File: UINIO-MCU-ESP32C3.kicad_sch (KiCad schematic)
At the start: 40 parts, among them J1 Conn_01x15_Male, J2 外接串行下载接口, J3 Conn_01x15_Male, SW1 复位按键, SW2 下载按键, U1 ME6211C33M5G-N, U2 W25Q128JVSSIQ, U3 ESP32-C3, U4 CH343P, Y1 40MHz

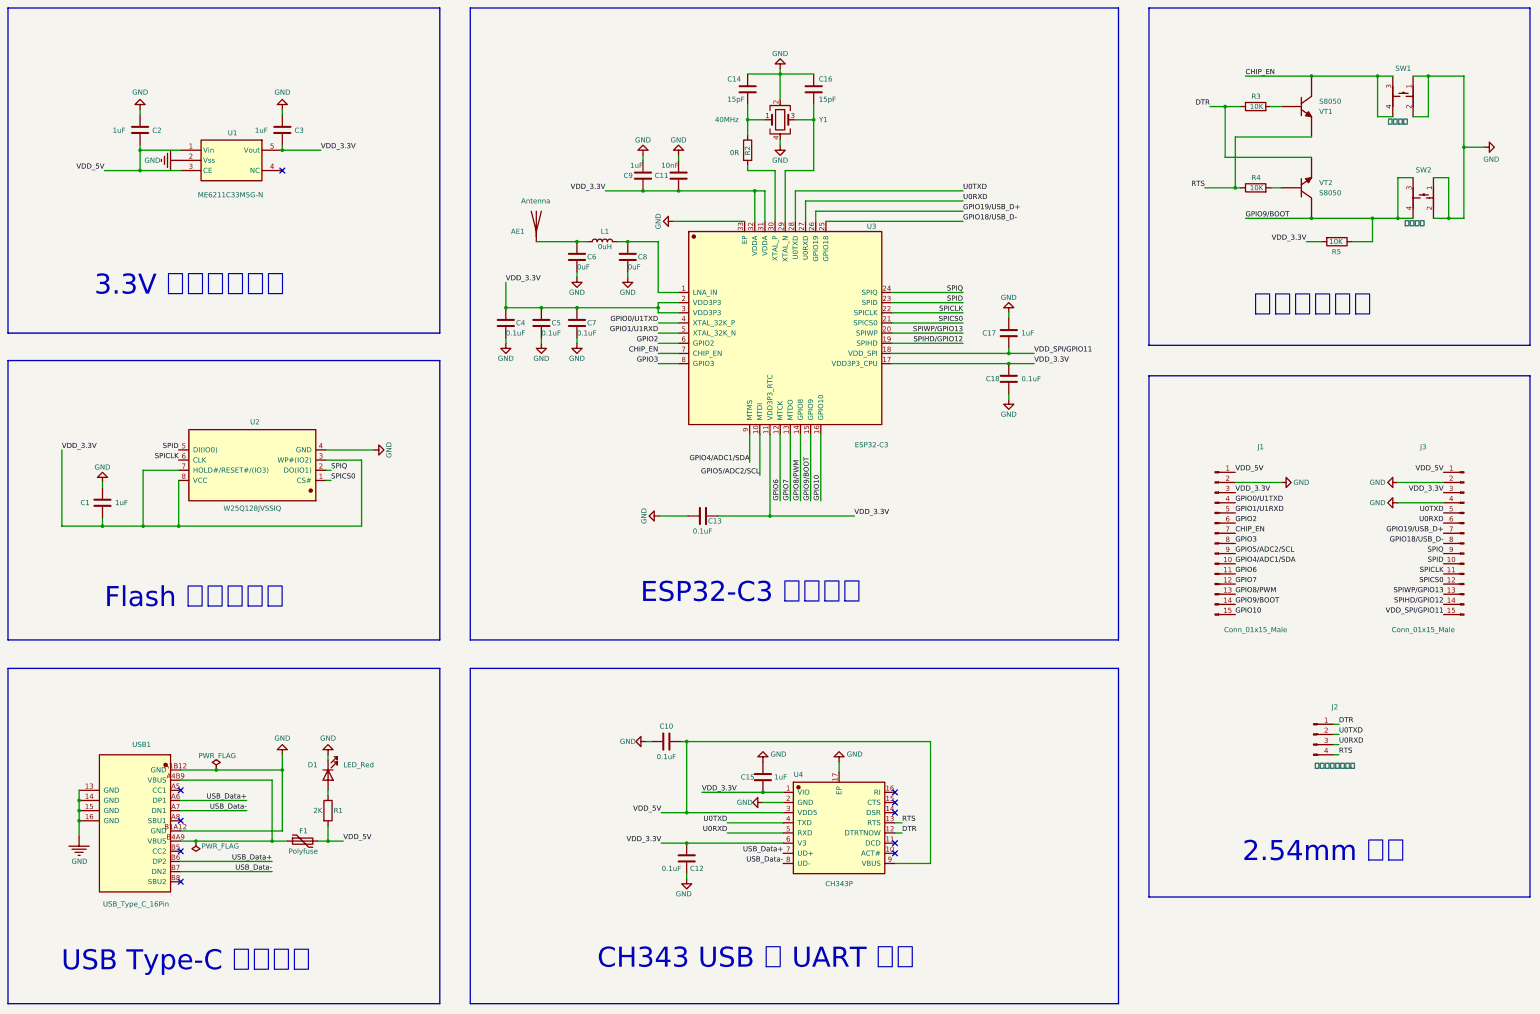
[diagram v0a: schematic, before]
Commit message: The schematic diagram is drawn.
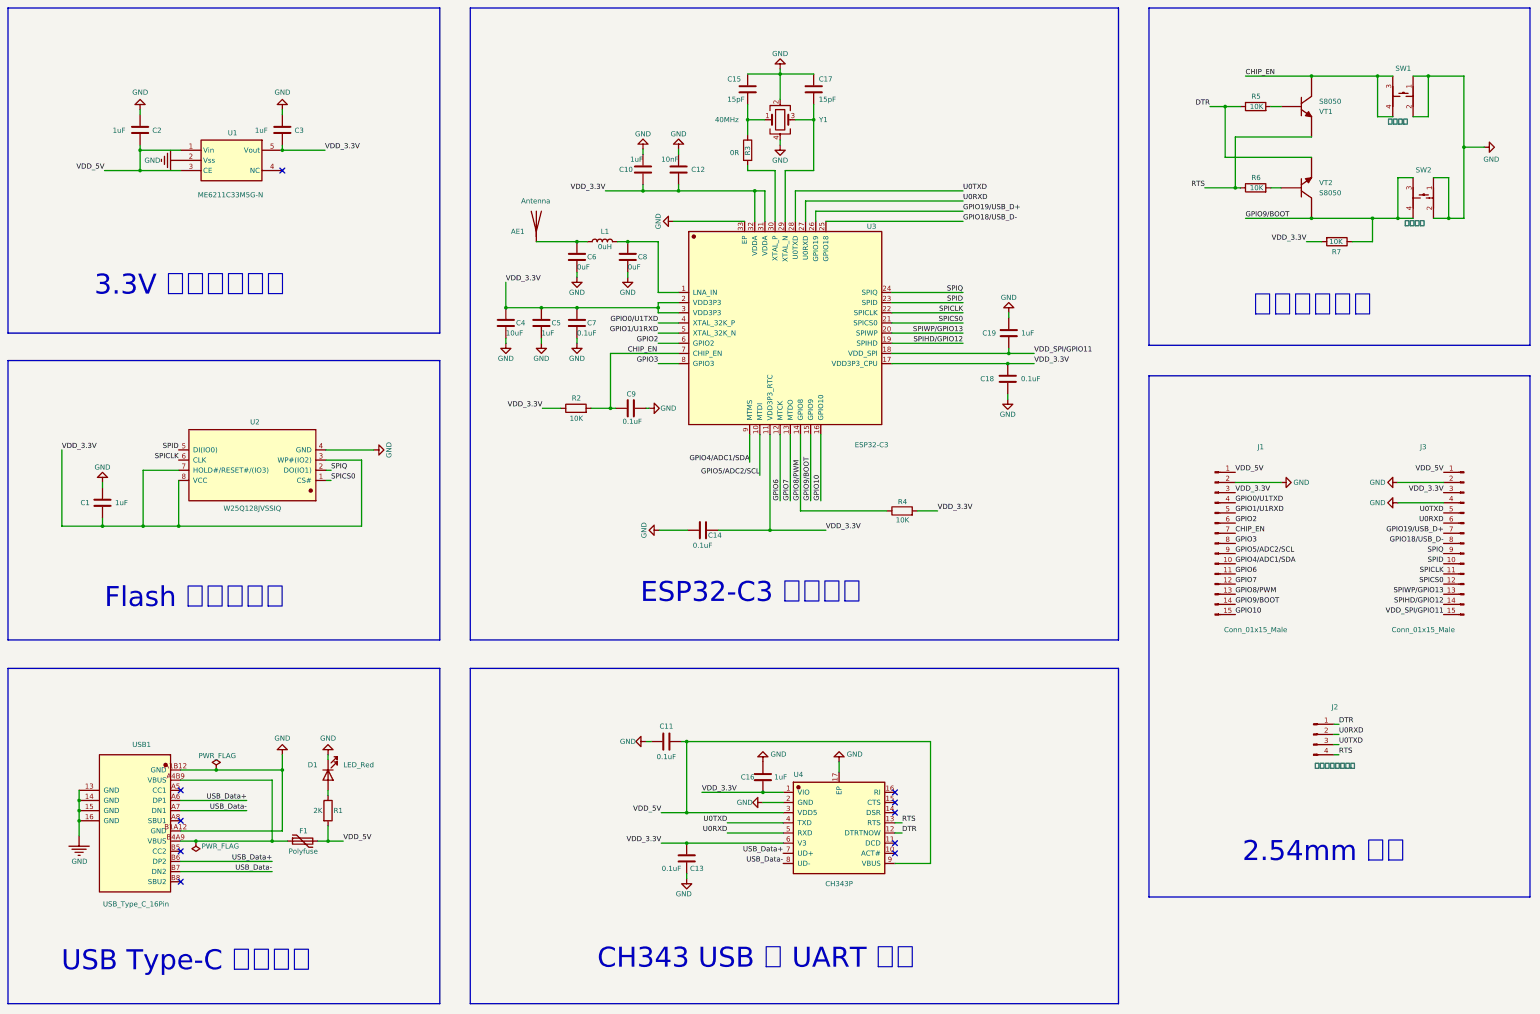
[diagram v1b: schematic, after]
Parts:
- added C9: 0.1uF, Capacitor_SMD:C_0402_1005Metric, symbol Device:C
- added R2, R4: 10K, Resistor_SMD:R_0402_1005Metric, symbol Device:R
- C4: value 0.1uF -> 10uF
- C5: value 0.1uF -> 1uF
- U1: footprint Uinio:SOT23-5 -> Uinio:SOT-23-5_L3.0-W1.7-P0.95-LS2.8-BR
- renumbered C9 to C10, C10 to C11, C11 to C12, C12 to C13, C13 to C14, C14 to C15, C15 to C16, C16 to C17, C17 to C19, R2 to R3, R3 to R5, R4 to R6, R5 to R7
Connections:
- net CHIP_EN: now also C9.1, R2.2
- net GND: now also C9.2
- net GPIO8/PWM: now also R4.1
- net U0RXD: now also J2.2 (Pin_2); no longer J2.3 (Pin_3)
- net U0TXD: now also J2.3 (Pin_3); no longer J2.2 (Pin_2)
- net VDD_3.3V: now also R2.1, R4.2
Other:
- moved on the sheet: C10, C12, C14

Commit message: Finish PCB Layout.
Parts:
- removed F1: Polyfuse, Fuse:Fuse_1206_3216Metric, symbol Device:Polyfuse
- removed R3: 0R, Resistor_SMD:R_0402_1005Metric, symbol Device:R
- AE1: footprint RF_Antenna:Texas_SWRA117D_2.4GHz_Left -> RF_Antenna:Texas_SWRA117D_2.4GHz_Right
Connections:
- net CHIP_EN: now also J1.5 (Pin_5); no longer J1.7 (Pin_7)
- net GND: now also J1.1 (Pin_1), J1.14 (Pin_14), J3.1 (Pin_1), J3.14 (Pin_14); no longer J1.2 (Pin_2), J3.2 (Pin_2), J3.4 (Pin_4)
- net GPIO0/U1TXD: now also J1.2 (Pin_2); no longer J1.4 (Pin_4)
- net GPIO10: now also J1.13 (Pin_13); no longer J1.15 (Pin_15)
- net GPIO18/USB_D-: now also J3.6 (Pin_6); no longer J3.8 (Pin_8)
- net GPIO19/USB_D+: now also J3.5 (Pin_5); no longer J3.7 (Pin_7)
- net GPIO1/U1RXD: now also J1.3 (Pin_3); no longer J1.5 (Pin_5)
- net GPIO2: now also J1.4 (Pin_4); no longer J1.6 (Pin_6)
- net GPIO3: now also J1.6 (Pin_6); no longer J1.8 (Pin_8)
- net GPIO4/ADC1/SDA: now also J1.8 (Pin_8); no longer J1.10 (Pin_10)
- net GPIO5/ADC2/SCL: now also J1.7 (Pin_7); no longer J1.9 (Pin_9)
- net GPIO6: now also J1.9 (Pin_9); no longer J1.11 (Pin_11)
- net GPIO7: now also J1.10 (Pin_10); no longer J1.12 (Pin_12)
- net GPIO8/PWM: now also J1.11 (Pin_11); no longer J1.13 (Pin_13)
- net GPIO9/BOOT: now also J1.12 (Pin_12); no longer J1.14 (Pin_14)
- net SPICLK: now also J3.9 (Pin_9); no longer J3.11 (Pin_11)
- net SPICS0: now also J3.10 (Pin_10); no longer J3.12 (Pin_12)
- net SPID: now also J3.8 (Pin_8); no longer J3.10 (Pin_10)
- net SPIHD/GPIO12: now also J3.12 (Pin_12); no longer J3.14 (Pin_14)
- net SPIQ: now also J3.7 (Pin_7); no longer J3.9 (Pin_9)
- net SPIWP/GPIO13: now also J3.11 (Pin_11); no longer J3.13 (Pin_13)
- net U0RXD: now also J3.4 (Pin_4); no longer J3.6 (Pin_6)
- net U0TXD: now also J3.3 (Pin_3); no longer J3.5 (Pin_5)
- net VDD_3.3V: now also J1.15 (Pin_15), J3.2 (Pin_2); no longer J1.3 (Pin_3), J3.3 (Pin_3)
- net VDD_5V: now also J3.15 (Pin_15), USB1.A4B9 (VBUS), USB1.B4A9 (VBUS); no longer J1.1 (Pin_1), J3.1 (Pin_1)
- net VDD_SPI/GPIO11: now also J3.13 (Pin_13); no longer J3.15 (Pin_15)
- net at C15.2, Y1.1: now also U3.30 (XTAL_P)
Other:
- moved on the sheet: AE1, C1, C10, C11, C12, C13, C14, C15, C16, C17, C18, C19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

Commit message: Finish PCB Layout.
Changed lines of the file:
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@@
     (stroke (width 0) (type default) (color 0 0 0 0))
   )
-  (wire (pts (xy 320.04 46.99) (xy 323.85 46.99))
+  (wire (pts (xy 318.516 46.99) (xy 323.85 46.99))
     (stroke (width 0) (type default) (color 0 0 0 0))
   )
@@
     (effects (font (size 1.27 1.27)) (justify right bottom))
   )
-  (label "DTR" (at 320.04 46.99 180)
-    (effects (font (size 1.27 1.27)) (justify right bottom))
-  )
+  (label "DTR" (at 318.516 46.99 180)
+    (effects (font (size 1.27 1.27)) (justify right bottom))
+  )

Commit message: Ready for release.
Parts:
- removed AE1: Antenna, RF_Antenna:Texas_SWRA117D_2.4GHz_Right, symbol Device:Antenna
- added AE1: Antenna_Dipole, RF_Antenna:Texas_SWRA117D_2.4GHz_Right, symbol Device:Antenna_Dipole
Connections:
- net GND: now also AE1.1
- net at C6.1, L1.1: now also AE1.2
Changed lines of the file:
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@@
+    (stroke (width 0) (type default) (color 0 0 0 0))
+  )
+  (wire (pts (xy 148.59 81.28) (xy 148.59 82.55))
     (stroke (width 0) (type default) (color 0 0 0 0))
   )
@@
   (symbol (lib_id "power:GND") (at 337.82 138.43 90) (unit 1)
     (in_bom yes) (on_board yes)
-    (property "Reference" "#PWR?" (id 0) (at 344.17 138.43 0)
+    (property "Reference" "#PWR032" (id 0) (at 344.17 138.43 0)
       (effects (font (size 1.27 1.27)) hide)
     )
@@
     )
     (property "Datasheet" "" (id 3) (at 337.82 171.45 0)
-      (effects (font (size 1.27 1.27)) hide)
-    )
-    (pin "1")
-  )
-  (symbol (lib_id "Device:Antenna") (at 151.13 76.2 0) (unit 1)
-    (in_bom yes) (on_board yes)
-    (property "Reference" "AE1" (id 0) (at 144.78 78.74 0)
-      (effects (font (size 1.27 1.27)) (justify left))
-    )
-    (property "Value" "Antenna" (id 1) (at 147.32 71.12 0)
-      (effects (font (size 1.27 1.27)) (justify left))
-    )
-    (property "Footprint" "RF_Antenna:Texas_SWRA117D_2.4GHz_Right" (id 2) (at 151.13 76.2 0)
-      (effects (font (size 1.27 1.27)) hide)
-    )
-    (property "Datasheet" "~" (id 3) (at 151.13 76.2 0)
       (effects (font (size 1.27 1.27)) hide)
     )
@@
     (pin "1")
   )
+  (symbol (lib_id "power:GND") (at 148.59 82.55 0) (unit 1)
+    (in_bom yes) (on_board yes)
+    (property "Reference" "#PWR0101" (id 0) (at 148.59 88.9 0)
+      (effects (font (size 1.27 1.27)) hide)
+    )
+    (property "Value" "GND" (id 1) (at 148.59 86.36 0))
+    (property "Footprint" "" (id 2) (at 148.59 82.55 0)
+      (effects (font (size 1.27 1.27)) hide)
+    )
+    (property "Datasheet" "" (id 3) (at 148.59 82.55 0)
+      (effects (font (size 1.27 1.27)) hide)
+    )
+    (pin "1")
+  )
   (symbol (lib_id "power:GND") (at 227.33 210.82 180) (unit 1)
     (in_bom yes) (on_board yes)
@@
     (pin "2")
   )
+  (symbol (lib_id "Device:Antenna_Dipole") (at 148.59 76.2 0) (unit 1)
+    (in_bom yes) (on_board yes)
+    (property "Reference" "AE1" (id 0) (at 142.875 81.28 0)
+      (effects (font (size 1.27 1.27)) (justify left))
+    )
+    (property "Value" "Antenna_Dipole" (id 1) (at 142.875 75.565 0)
+      (effects (font (size 1.27 1.27)) (justify left))
+    )
+    (property "Footprint" "RF_Antenna:Texas_SWRA117D_2.4GHz_Right" (id 2) (at 148.59 76.2 0)
+      (effects (font (size 1.27 1.27)) hide)
+    )
+    (property "Datasheet" "~" (id 3) (at 148.59 76.2 0)
+      (effects (font (size 1.27 1.27)) hide)
+    )
+    (pin "1")
+    (pin "2")
+  )
   (symbol (lib_id "power:GND") (at 179.07 121.92 90) (unit 1)
     (in_bom yes) (on_board yes)
@@
     )
     (path "/58e2e744-8591-4d2c-9aac-61870cbfde6c"
-      (reference "#PWR?") (unit 1) (value "GND") (footprint "")
-    )
-    (path "/64ebc70a-a297-448d-8134-99cc5b0fa170"
-      (reference "AE1") (unit 1) (value "Antenna") (footprint "RF_Antenna:Texas_SWRA117D_2.4GHz_Right")
+      (reference "#PWR032") (unit 1) (value "GND") (footprint "")
+    )
+    (path "/c256f872-eb62-436c-b82d-9e745c05524a"
+      (reference "#PWR0101") (unit 1) (value "GND") (footprint "")
+    )
+    (path "/def514a0-07a4-44d2-9c16-a6e669a7c211"
+      (reference "AE1") (unit 1) (value "Antenna_Dipole") (footprint "RF_Antenna:Texas_SWRA117D_2.4GHz_Right")
     )
     (path "/60a36da2-88ef-40da-90a3-fd1a0310b71d"

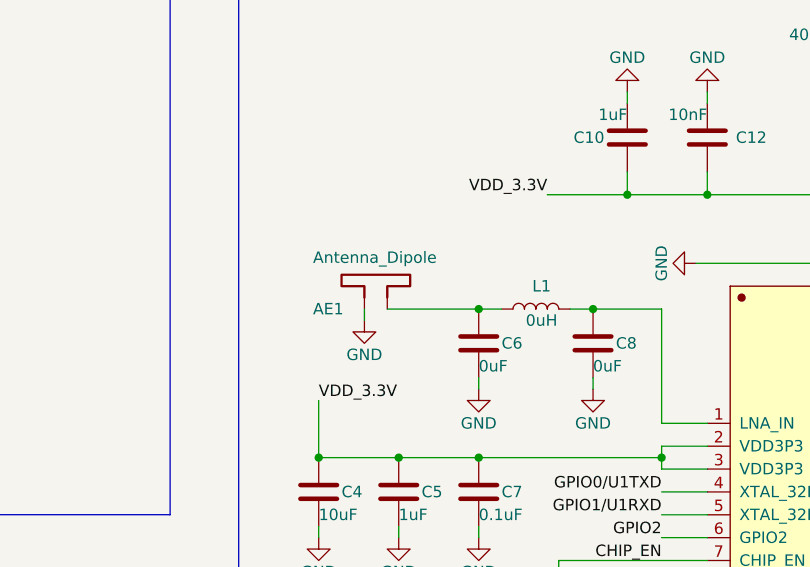
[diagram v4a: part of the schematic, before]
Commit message: Release UINIO-MCU-ESP32C3 version 1.0.0.
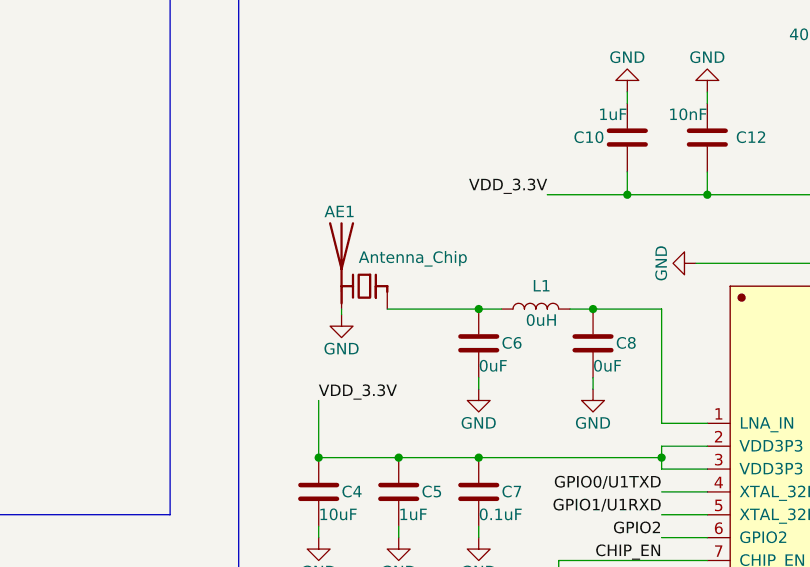
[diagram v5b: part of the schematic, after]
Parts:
- removed AE1: Antenna_Dipole, RF_Antenna:Texas_SWRA117D_2.4GHz_Right, symbol Device:Antenna_Dipole
- added AE1: Antenna_Chip, RF_Antenna:Texas_SWRA117D_2.4GHz_Right, symbol Device:Antenna_Chip
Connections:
- net GND: now also AE1.2 (PCB_Trace)
- net at C6.1, L1.1: now also AE1.1 (FEED)
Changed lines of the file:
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@@
   (title_block
     (title "UINIO-MCU-ESP32C3")
-    (date "2022-12-01")
+    (date "2022-12-08")
     (rev "Version 1.0.0")
     (company "电子技术博客 UinIO.com")
@@
     (stroke (width 0) (type default) (color 0 0 0 0))
   )
-  (wire (pts (xy 148.59 81.28) (xy 148.59 82.55))
+  (wire (pts (xy 146.05 81.28) (xy 146.05 81.915))
     (stroke (width 0) (type default) (color 0 0 0 0))
   )
@@
     )
     (pin "1")
+  )
+  (symbol (lib_id "Device:Antenna_Chip") (at 148.59 78.74 0) (mirror y) (unit 1)
+    (in_bom yes) (on_board yes)
+    (property "Reference" "AE1" (id 0) (at 144.145 70.485 0)
+      (effects (font (size 1.27 1.27)) (justify right))
+    )
+    (property "Value" "Antenna_Chip" (id 1) (at 147.955 75.565 0)
+      (effects (font (size 1.27 1.27)) (justify right))
+    )
+    (property "Footprint" "RF_Antenna:Texas_SWRA117D_2.4GHz_Right" (id 2) (at 151.13 74.295 0)
+      (effects (font (size 1.27 1.27)) hide)
+    )
+    (property "Datasheet" "~" (id 3) (at 151.13 74.295 0)
+      (effects (font (size 1.27 1.27)) hide)
+    )
+    (pin "1")
+    (pin "2")
   )
   (symbol (lib_id "Device:C") (at 175.26 121.92 90) (unit 1)
@@
     (pin "1")
   )
-  (symbol (lib_id "power:GND") (at 148.59 82.55 0) (unit 1)
-    (in_bom yes) (on_board yes)
-    (property "Reference" "#PWR0101" (id 0) (at 148.59 88.9 0)
-      (effects (font (size 1.27 1.27)) hide)
-    )
-    (property "Value" "GND" (id 1) (at 148.59 86.36 0))
-    (property "Footprint" "" (id 2) (at 148.59 82.55 0)
-      (effects (font (size 1.27 1.27)) hide)
-    )
-    (property "Datasheet" "" (id 3) (at 148.59 82.55 0)
+  (symbol (lib_id "power:GND") (at 146.05 81.915 0) (unit 1)
+    (in_bom yes) (on_board yes)
+    (property "Reference" "#PWR0101" (id 0) (at 146.05 88.265 0)
+      (effects (font (size 1.27 1.27)) hide)
+    )
+    (property "Value" "GND" (id 1) (at 146.05 85.725 0))
+    (property "Footprint" "" (id 2) (at 146.05 81.915 0)
+      (effects (font (size 1.27 1.27)) hide)
+    )
+    (property "Datasheet" "" (id 3) (at 146.05 81.915 0)
       (effects (font (size 1.27 1.27)) hide)
     )
@@
     (pin "2")
   )
-  (symbol (lib_id "Device:Antenna_Dipole") (at 148.59 76.2 0) (unit 1)
-    (in_bom yes) (on_board yes)
-    (property "Reference" "AE1" (id 0) (at 142.875 81.28 0)
-      (effects (font (size 1.27 1.27)) (justify left))
-    )
-    (property "Value" "Antenna_Dipole" (id 1) (at 142.875 75.565 0)
-      (effects (font (size 1.27 1.27)) (justify left))
-    )
-    (property "Footprint" "RF_Antenna:Texas_SWRA117D_2.4GHz_Right" (id 2) (at 148.59 76.2 0)
-      (effects (font (size 1.27 1.27)) hide)
-    )
-    (property "Datasheet" "~" (id 3) (at 148.59 76.2 0)
-      (effects (font (size 1.27 1.27)) hide)
-    )
-    (pin "1")
-    (pin "2")
-  )
   (symbol (lib_id "power:GND") (at 179.07 121.92 90) (unit 1)
     (in_bom yes) (on_board yes)
@@
       (reference "#PWR0101") (unit 1) (value "GND") (footprint "")
     )
-    (path "/def514a0-07a4-44d2-9c16-a6e669a7c211"
-      (reference "AE1") (unit 1) (value "Antenna_Dipole") (footprint "RF_Antenna:Texas_SWRA117D_2.4GHz_Right")
+    (path "/1270280a-55c4-4f77-a089-69511146a306"
+      (reference "AE1") (unit 1) (value "Antenna_Chip") (footprint "RF_Antenna:Texas_SWRA117D_2.4GHz_Right")
     )
     (path "/60a36da2-88ef-40da-90a3-fd1a0310b71d"

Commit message: Fix bug.
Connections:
- net U0RXD: now also U4.4 (TXD); no longer U4.5 (RXD)
- net U0TXD: now also U4.5 (RXD); no longer U4.4 (TXD)
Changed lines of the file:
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@@
     (effects (font (size 1.27 1.27)) (justify right bottom))
   )
-  (label "U0RXD" (at 199.39 228.6 180)
+  (label "U0RXD" (at 199.39 226.06 180)
     (effects (font (size 1.27 1.27)) (justify right bottom))
   )
@@
     (effects (font (size 1.27 1.27)) (justify right bottom))
   )
-  (label "U0TXD" (at 199.39 226.06 180)
+  (label "U0TXD" (at 199.39 228.6 180)
     (effects (font (size 1.27 1.27)) (justify right bottom))
   )

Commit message: Prepare version 3.0.0.
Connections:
- net VDD_3.3V: now also R1.2
- net VDD_5V: no longer R1.2
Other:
- moved on the sheet: C2, C3, D1, R1, U1, USB1
